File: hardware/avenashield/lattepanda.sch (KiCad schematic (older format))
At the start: 18 parts, among them J10 Lattepanda Lower Left Header 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, J11 12V DC IN Headers, J6 Lattepanda Upper Left Header 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, J7 Lattepanda Upper Right Header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, J8 Lattepanda Middle Left Header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, J9 Lattepanda Lower Right Header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, U8 TLC59108xPW

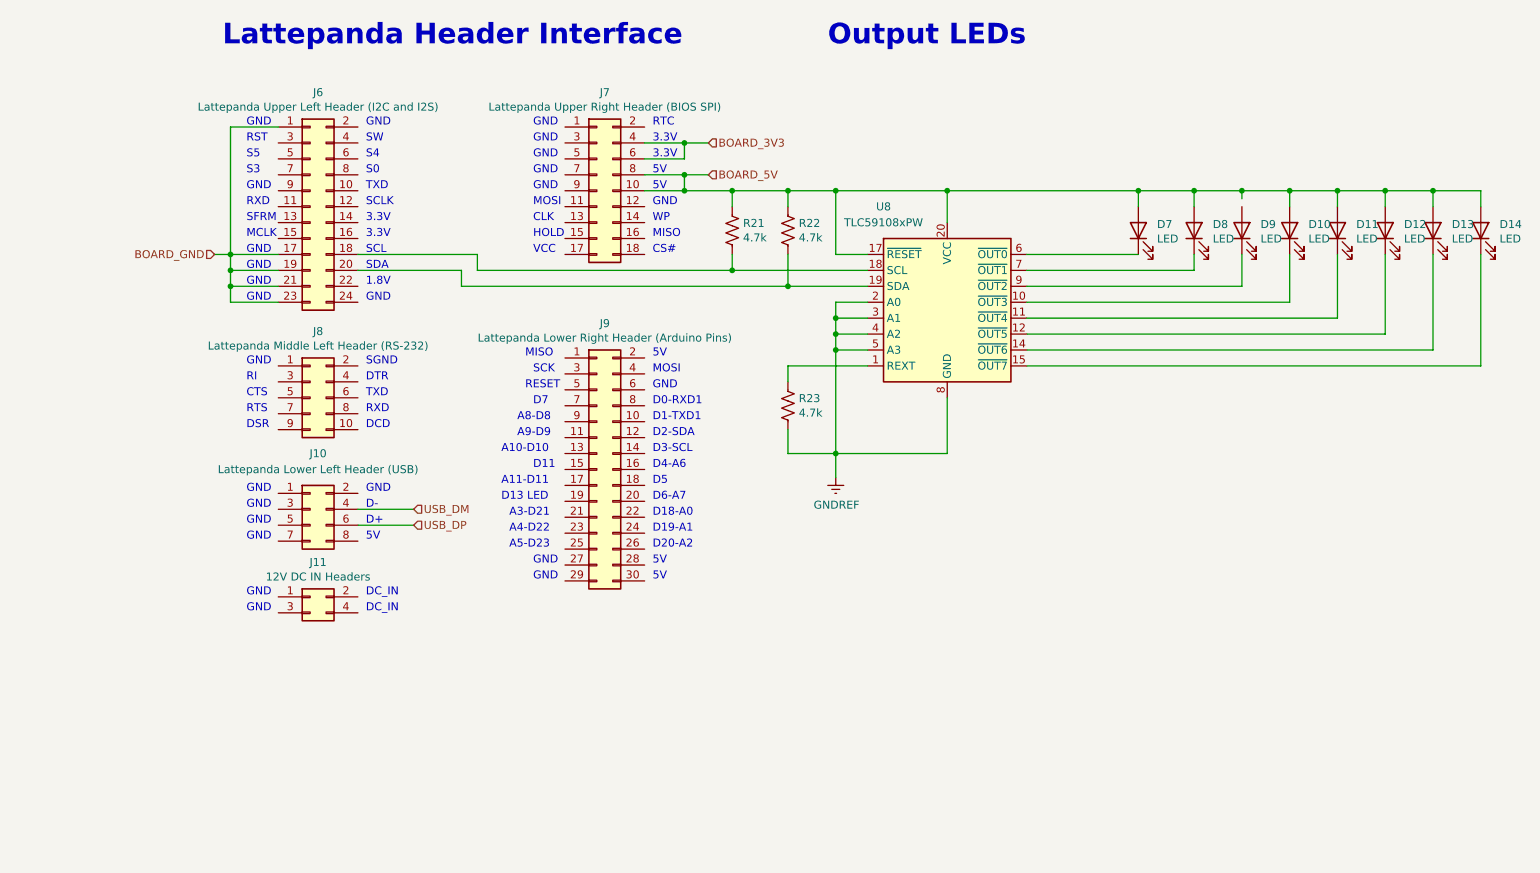
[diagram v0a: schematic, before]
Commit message: Added MiniPCIe latch clip and replaced onboard LEDs with connector
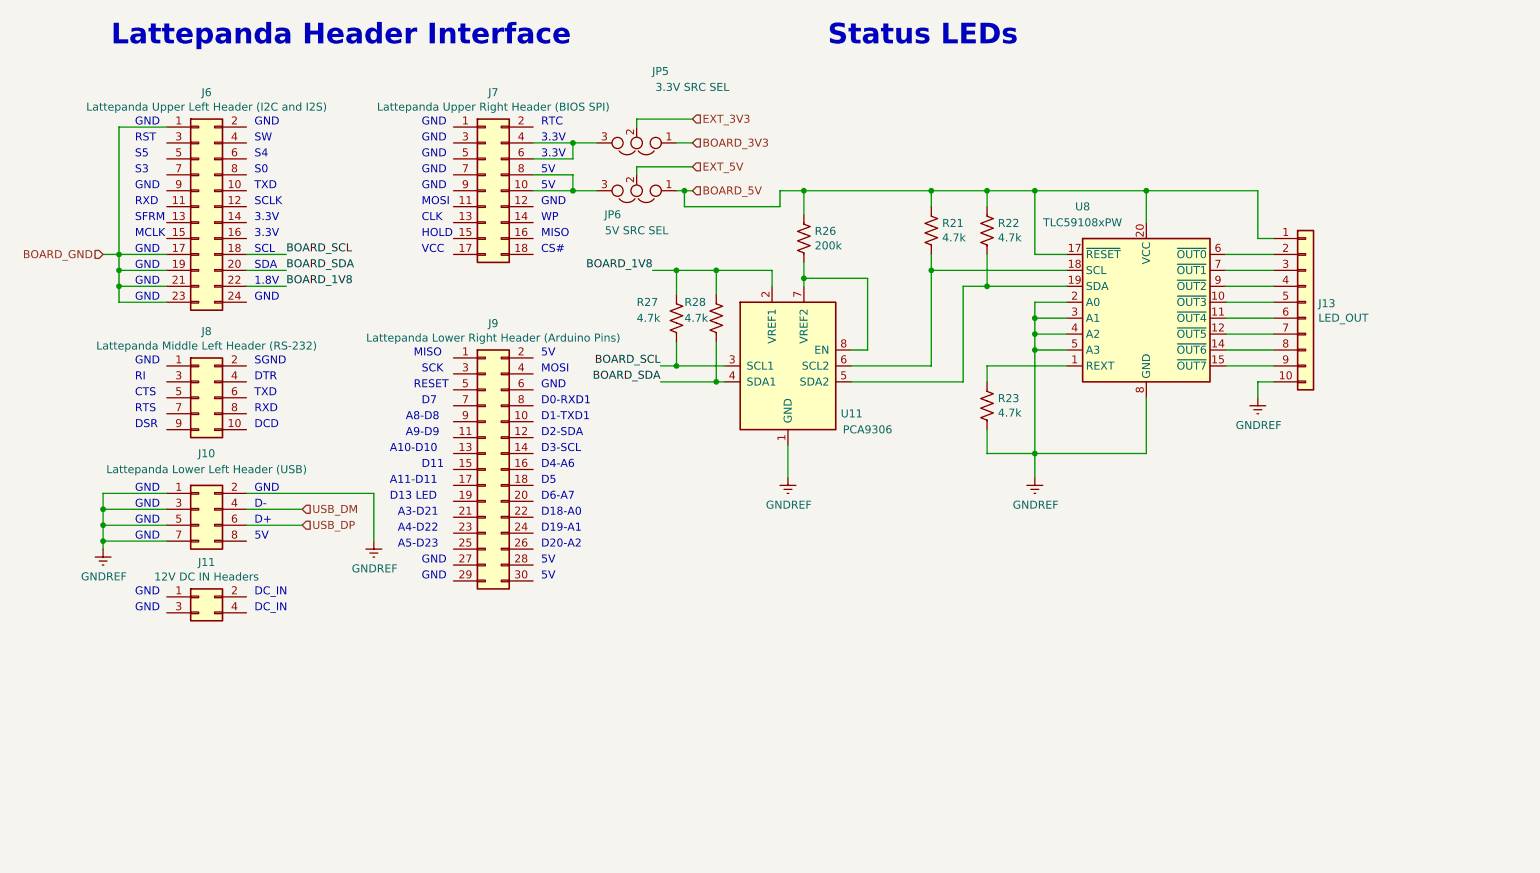
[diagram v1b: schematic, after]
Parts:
- removed D10, D11, D12, D13, D14, D7, D8, D9: LED, LED_SMD:LED_0805_2012Metric_Castellated, symbol Device:LED
- added J13: LED_OUT, Connector_PinHeader_2.54mm:PinHeader_2x05_P2.54mm_Horizontal, symbol Connector_Generic:Conn_01x10
- added JP5: 3.3V SRC SEL, Connector_PinHeader_2.54mm:PinHeader_1x03_P2.54mm_Vertical_SMD_Pin1Left, symbol Device:Jumper_NC_Dual
- added JP6: 5V SRC SEL, Connector_PinHeader_2.54mm:PinHeader_1x03_P2.54mm_Vertical_SMD_Pin1Left, symbol Device:Jumper_NC_Dual
- added R26: 200k, Resistor_SMD:R_1206_3216Metric, symbol Device:R_US
- added R27, R28: 4.7k, Resistor_SMD:R_1206_3216Metric, symbol Device:R_US
- added U11: PCA9306, Package_SO:SSOP-8_2.95x2.8mm_P0.65mm, symbol Interface:PCA9306
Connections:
- net BOARD_3V3: now also JP5.1; no longer J7.4 (Pin_4), J7.6 (Pin_6)
- net BOARD_5V: now also J13.1 (Pin_1), JP6.1, R26.1; no longer J7.10 (Pin_10), J7.8 (Pin_8)
- net GNDREF: now also J10.1 (Pin_1), J10.2 (Pin_2), J10.3 (Pin_3), J10.5 (Pin_5), J10.7 (Pin_7), J13.10 (Pin_10), U11.1 (GND)
- net at R21.2, U8.18 (SCL): now also U11.6 (SCL2); no longer J6.18 (Pin_18)
- net at R22.2, U8.19 (SDA): now also U11.5 (SDA2); no longer J6.20 (Pin_20)
- net BOARD_1V8: now reaches J6.22 (Pin_22)
- net BOARD_1V8: now also R27.1, R28.1, U11.2 (VREF1)
- net at U8.10 (~OUT3): now also J13.5 (Pin_5)
- net at U8.11 (~OUT4): now also J13.6 (Pin_6)
- net at U8.12 (~OUT5): now also J13.7 (Pin_7)
- net at U8.14 (~OUT6): now also J13.8 (Pin_8)
- net at U8.15 (~OUT7): now also J13.9 (Pin_9)
- net at U8.6 (~OUT0): now also J13.2 (Pin_2)
- net at U8.7 (~OUT1): now also J13.3 (Pin_3)
- net at U8.9 (~OUT2): now also J13.4 (Pin_4)
- new net: J7.10 (Pin_10), J7.8 (Pin_8), JP6.3
- new net: J7.4 (Pin_4), J7.6 (Pin_6), JP5.3
- new net: R26.2, U11.7 (VREF2), U11.8 (EN)
- new net BOARD_SCL: J6.18 (Pin_18), R27.2, U11.3 (SCL1)
- new net BOARD_SDA: J6.20 (Pin_20), R28.2, U11.4 (SDA1)
- new net EXT_3V3: JP5.2
- new net EXT_5V: JP6.2
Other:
- note added: "Status LEDs"
- note removed: "Output LEDs"
- moved on the sheet: J10, J11, J6, J7, J8, J9, R21, R22, R23, U8

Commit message: Changed footprints for CAN connectors and replaced 3D models for headers
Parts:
- R26: footprint Resistor_SMD:R_1206_3216Metric -> Resistor_SMD:R_0805_2012Metric_Pad1.15x1.40mm_HandSolder
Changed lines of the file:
@@
 F 0 "R26" H 5468 2146 50  0000 L CNN
 F 1 "200k" H 5468 2055 50  0000 L CNN
-F 2 "Resistor_SMD:R_1206_3216Metric" V 5440 2090 50  0001 C CNN
+F 2 "Resistor_SMD:R_0805_2012Metric_Pad1.15x1.40mm_HandSolder" V 5440 2090 50  0001 C CNN
 F 3 "~" H 5400 2100 50  0001 C CNN
 	1    5400 2100
@@
 	8250 2100 8250 1800
 $Comp
-L power:GNDREF #PWR?
+L power:GNDREF #PWR0197
 U 1 1 5F150078
 P 8250 3100
-F 0 "#PWR?" H 8250 2850 50  0001 C CNN
+F 0 "#PWR0197" H 8250 2850 50  0001 C CNN
 F 1 "GNDREF" H 8255 2927 50  0000 C CNN
 F 2 "" H 8250 3100 50  0001 C CNN

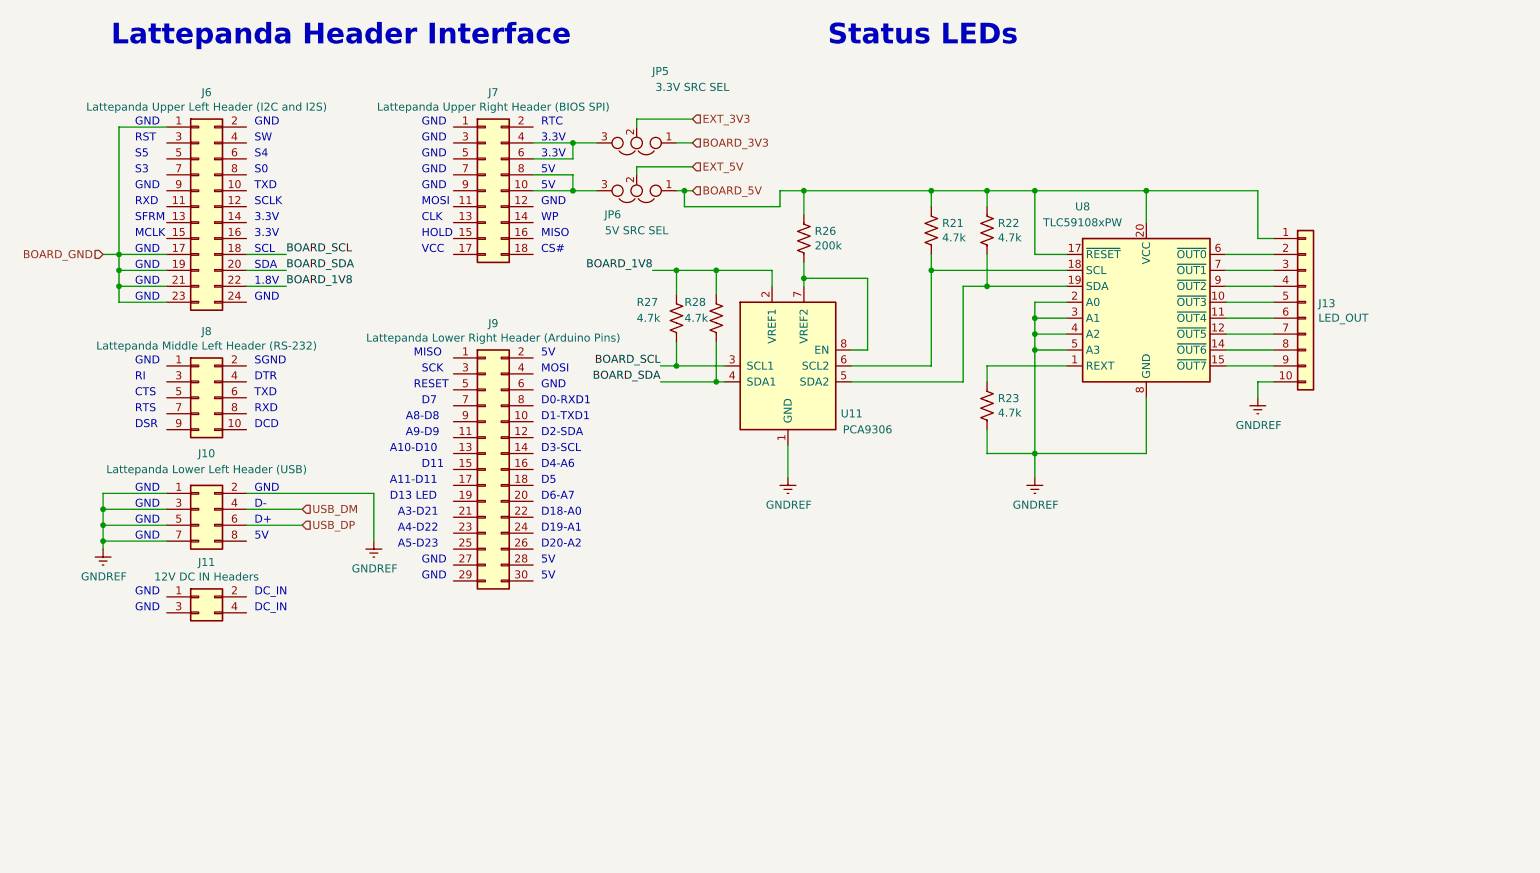
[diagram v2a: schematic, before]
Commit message: Improved I2C bus routing
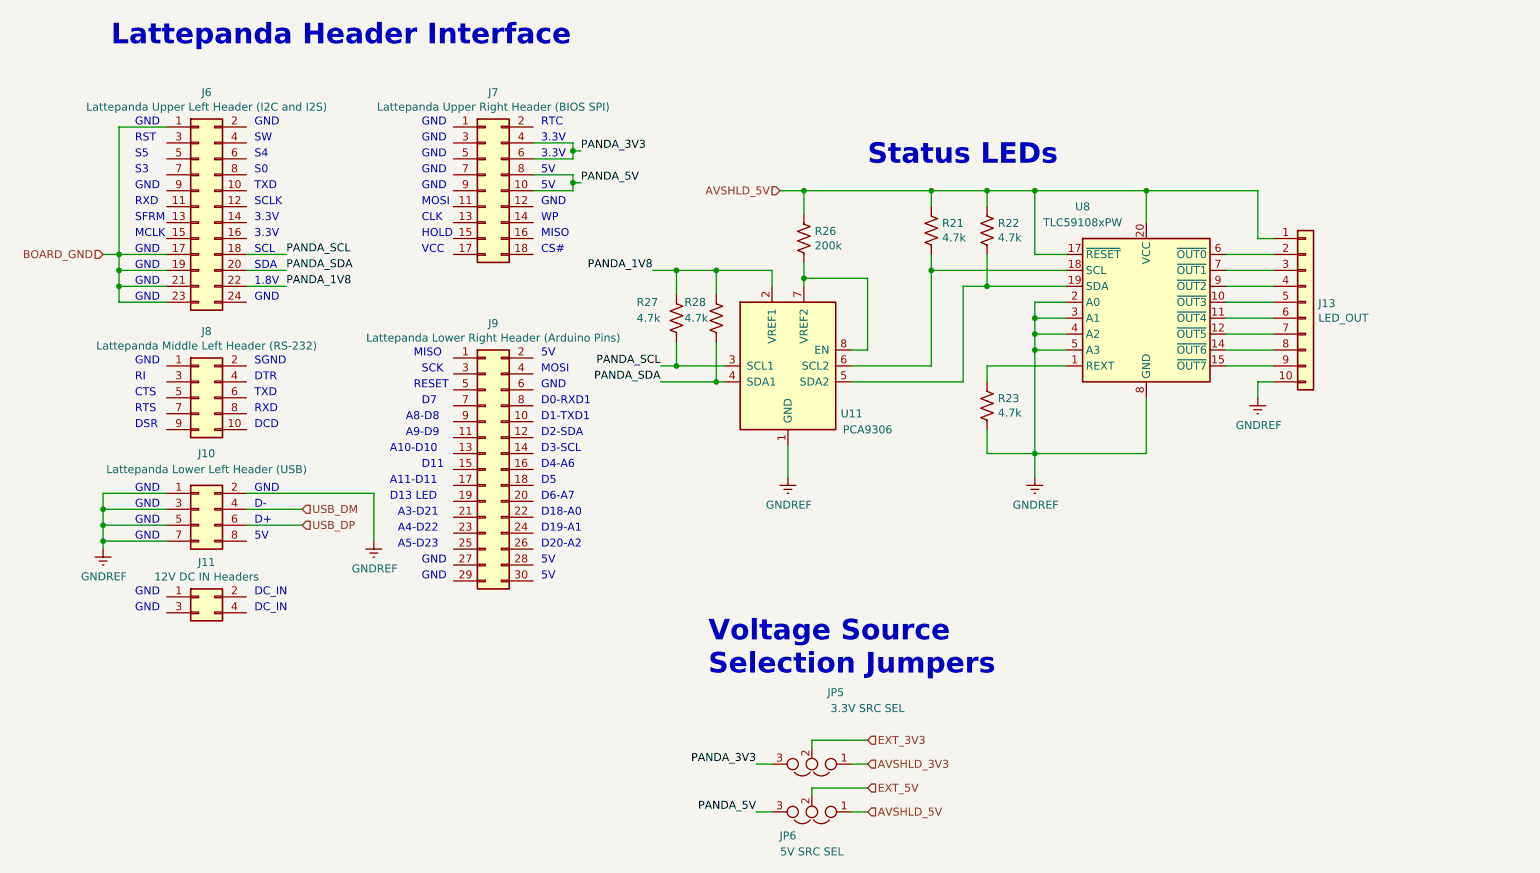
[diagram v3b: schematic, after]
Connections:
- net PANDA_5V: now reaches J7.10 (Pin_10), J7.8 (Pin_8), JP6.3
- net PANDA_3V3: now reaches J7.4 (Pin_4), J7.6 (Pin_6), JP5.3
- net BOARD_1V8 renamed PANDA_1V8
- net BOARD_3V3 renamed AVSHLD_3V3
- net BOARD_5V renamed AVSHLD_5V
- net BOARD_SCL renamed PANDA_SCL
- net BOARD_SDA renamed PANDA_SDA
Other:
- note added: "Voltage Source \nSelection Jumpers\n"
- moved on the sheet: JP5, JP6
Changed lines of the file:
@@
 Wire Wire Line
 	2250 3900 1900 3900
-Text HLabel 4700 1500 2    50   Input ~ 0
-BOARD_3V3
-Text HLabel 4700 1800 2    50   Input ~ 0
-BOARD_5V
+Text HLabel 5800 5400 2    50   Input ~ 0
+AVSHLD_3V3
+Text HLabel 5800 5700 2    50   Input ~ 0
+AVSHLD_5V
 Wire Wire Line
 	3700 1600 3950 1600
 Wire Wire Line
-	3950 1600 3950 1500
+	3950 1600 3950 1550
 Wire Wire Line
 	3950 1500 3700 1500
 Wire Wire Line
-	3950 1700 3950 1800
+	3950 1700 3950 1750
 Wire Wire Line
 	3950 1800 3700 1800
@@
 Text Notes 1050 900  0    129  ~ 26
 Lattepanda Header Interface
-Text Notes 5550 900  0    129  ~ 26
+Text Notes 5800 1650 0    129  ~ 26
 Status LEDs
 $Comp
@@
 Connection ~ 6200 1800
 Text Label 2150 2200 0    50   ~ 0
-BOARD_SCL
+PANDA_SCL
 Text Label 2150 2300 0    50   ~ 0
-BOARD_SDA
+PANDA_SDA
 Text Label 2150 2400 0    50   ~ 0
-BOARD_1V8
+PANDA_1V8
 Wire Wire Line
 	2150 2200 1900 2200
@@
 	1900 2400 2150 2400
 Text Label 4500 2900 2    50   ~ 0
-BOARD_SCL
+PANDA_SCL
 Text Label 4500 3000 2    50   ~ 0
-BOARD_SDA
+PANDA_SDA
 Wire Wire Line
 	4500 2900 4600 2900
@@
 	4900 3000 4850 3000
 Text Label 4450 2300 2    50   ~ 0
-BOARD_1V8
+PANDA_1V8
 Wire Wire Line
 	4450 2300 4600 2300
@@
 L Device:Jumper_NC_Dual JP6
 U 1 1 5E6D8CB0
-P 4350 1800
-F 0 "JP6" H 4500 1950 50  0000 C CNN
-F 1 "5V SRC SEL" H 4350 2050 50  0000 C CNN
-F 2 "Connector_PinHeader_2.54mm:PinHeader_1x03_P2.54mm_Vertical_SMD_Pin1Left" H 4350 1800 50  0001 C CNN
-F 3 "~" H 4350 1800 50  0001 C CNN
-	1    4350 1800
+P 5450 5700
+F 0 "JP6" H 5600 5850 50  0000 C CNN
+F 1 "5V SRC SEL" H 5450 5950 50  0000 C CNN
+F 2 "Connector_PinHeader_2.54mm:PinHeader_1x03_P2.54mm_Vertical_SMD_Pin1Left" H 5450 5700 50  0001 C CNN
+F 3 "~" H 5450 5700 50  0001 C CNN
+	1    5450 5700
 	-1   0    0    1
 $EndComp
@@
 L Device:Jumper_NC_Dual JP5
 U 1 1 5E6E8EC7
-P 4350 1500
-F 0 "JP5" H 4200 1050 50  0000 C CNN
-F 1 "3.3V SRC SEL" H 4000 1150 50  0000 C CNN
-F 2 "Connector_PinHeader_2.54mm:PinHeader_1x03_P2.54mm_Vertical_SMD_Pin1Left" H 4350 1500 50  0001 C CNN
-F 3 "~" H 4350 1500 50  0001 C CNN
-	1    4350 1500
+P 5450 5400
+F 0 "JP5" H 5300 4950 50  0000 C CNN
+F 1 "3.3V SRC SEL" H 5100 5050 50  0000 C CNN
+F 2 "Connector_PinHeader_2.54mm:PinHeader_1x03_P2.54mm_Vertical_SMD_Pin1Left" H 5450 5400 50  0001 C CNN
+F 3 "~" H 5450 5400 50  0001 C CNN
+	1    5450 5400
 	-1   0    0    1
 $EndComp
 Wire Wire Line
-	3950 1500 4100 1500
-Connection ~ 3950 1500
-Wire Wire Line
-	4600 1500 4700 1500
-Wire Wire Line
-	4700 1800 4650 1800
-Wire Wire Line
-	4650 1800 4650 1900
-Wire Wire Line
-	4650 1900 5250 1900
-Wire Wire Line
-	5250 1900 5250 1800
+	5700 5400 5800 5400
 Wire Wire Line
 	5250 1800 5400 1800
-Connection ~ 4650 1800
-Wire Wire Line
-	4650 1800 4600 1800
 Connection ~ 5400 1800
-Wire Wire Line
-	4100 1800 3950 1800
-Connection ~ 3950 1800
-Text HLabel 4700 1350 2    50   Input ~ 0
+Text HLabel 5800 5250 2    50   Input ~ 0
 EXT_3V3
-Text HLabel 4700 1650 2    50   Input ~ 0
+Text HLabel 5800 5550 2    50   Input ~ 0
 EXT_5V
 Wire Wire Line
-	4700 1350 4350 1350
-Wire Wire Line
-	4350 1350 4350 1400
-Wire Wire Line
-	4700 1650 4350 1650
-Wire Wire Line
-	4350 1650 4350 1700
+	5800 5250 5450 5250
+Wire Wire Line
+	5450 5250 5450 5300
+Wire Wire Line
+	5800 5550 5450 5550
+Wire Wire Line
+	5450 5550 5450 5600
 $Comp
 L power:GNDREF #PWR0140
@@
 Wire Wire Line
 	8250 3000 8350 3000
+Wire Wire Line
+	5700 5700 5800 5700
+Text Label 4000 1550 0    50   ~ 0
+PANDA_3V3
+Text Label 4000 1750 0    50   ~ 0
+PANDA_5V
+Wire Wire Line
+	4000 1550 3950 1550
+Connection ~ 3950 1550
+Wire Wire Line
+	3950 1550 3950 1500
+Wire Wire Line
+	4000 1750 3950 1750
+Connection ~ 3950 1750
+Wire Wire Line
+	3950 1750 3950 1800
+Text Label 5100 5400 2    50   ~ 0
+PANDA_3V3
+Text Label 5100 5700 2    50   ~ 0
+PANDA_5V
+Wire Wire Line
+	5100 5400 5200 5400
+Wire Wire Line
+	5100 5700 5200 5700
+Text Notes 4800 4850 0    129  ~ 26
+Voltage Source \nSelection Jumpers\n
+Text HLabel 5250 1800 0    50   Input ~ 0
+AVSHLD_5V
 $EndSCHEMATC
